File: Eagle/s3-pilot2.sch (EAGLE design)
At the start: 17 parts, among them J1 ARDUINO_R3_SHIELD, M2_1 ENA_JMP

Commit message: chkpt before changing ISR around - it is not working well - too fast?
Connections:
- new net 3.3: J1.3.3V, MPU6050.VCC
- net GND: now also J1.GND@0, J1.GND@1
- net VDD: no longer MPU6050.VCC
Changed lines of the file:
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@@
 <wire x1="241.3" y1="38.1" x2="241.3" y2="81.28" width="0.1524" layer="91"/>
 <pinref part="J1" gate="G$1" pin="GND@2"/>
-<wire x1="241.3" y1="81.28" x2="223.52" y2="81.28" width="0.1524" layer="91"/>
+<wire x1="241.3" y1="81.28" x2="228.6" y2="81.28" width="0.1524" layer="91"/>
+<wire x1="228.6" y1="81.28" x2="223.52" y2="81.28" width="0.1524" layer="91"/>
 <wire x1="241.3" y1="81.28" x2="241.3" y2="86.36" width="0.1524" layer="91"/>
 <junction x="241.3" y="81.28"/>
 <pinref part="GND2" gate="1" pin="GND"/>
+<pinref part="J1" gate="G$1" pin="GND@0"/>
+<wire x1="223.52" y1="86.36" x2="228.6" y2="86.36" width="0.1524" layer="91"/>
+<wire x1="228.6" y1="86.36" x2="228.6" y2="83.82" width="0.1524" layer="91"/>
+<junction x="228.6" y="81.28"/>
+<pinref part="J1" gate="G$1" pin="GND@1"/>
+<wire x1="228.6" y1="83.82" x2="228.6" y2="81.28" width="0.1524" layer="91"/>
+<wire x1="223.52" y1="83.82" x2="228.6" y2="83.82" width="0.1524" layer="91"/>
+<junction x="228.6" y="83.82"/>
 </segment>
 <segment>
@@
 <net name="VDD" class="1">
 <segment>
-<pinref part="MPU6050" gate="G$1" pin="VCC"/>
-<wire x1="160.02" y1="35.56" x2="243.84" y2="35.56" width="0.1524" layer="91"/>
-<wire x1="243.84" y1="35.56" x2="243.84" y2="73.66" width="0.1524" layer="91"/>
+<wire x1="243.84" y1="30.48" x2="243.84" y2="73.66" width="0.1524" layer="91"/>
 <pinref part="J1" gate="G$1" pin="5V"/>
 <wire x1="243.84" y1="73.66" x2="223.52" y2="73.66" width="0.1524" layer="91"/>
-<wire x1="243.84" y1="35.56" x2="243.84" y2="30.48" width="0.1524" layer="91"/>
-<junction x="243.84" y="35.56"/>
 <pinref part="SUPPLY1" gate="VDD" pin="VDD"/>
 </segment>
@@
 </segment>
 </net>
+<net name="3.3" class="0">
+<segment>
+<pinref part="J1" gate="G$1" pin="3.3V"/>
+<wire x1="223.52" y1="76.2" x2="228.6" y2="76.2" width="0.1524" layer="91"/>
+<label x="228.6" y="76.2" size="1.778" layer="95"/>
+</segment>
+<segment>
+<pinref part="MPU6050" gate="G$1" pin="VCC"/>
+<wire x1="160.02" y1="35.56" x2="170.18" y2="35.56" width="0.1524" layer="91"/>
+<label x="165.1" y="35.56" size="1.778" layer="95"/>
+</segment>
+</net>

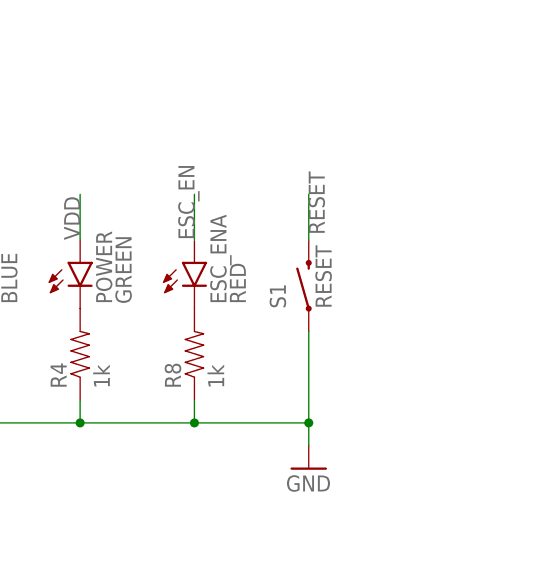
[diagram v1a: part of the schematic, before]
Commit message: working basically, still need to correct x/y/h stuff (as usual) added remote reset jumper for arduino to sch
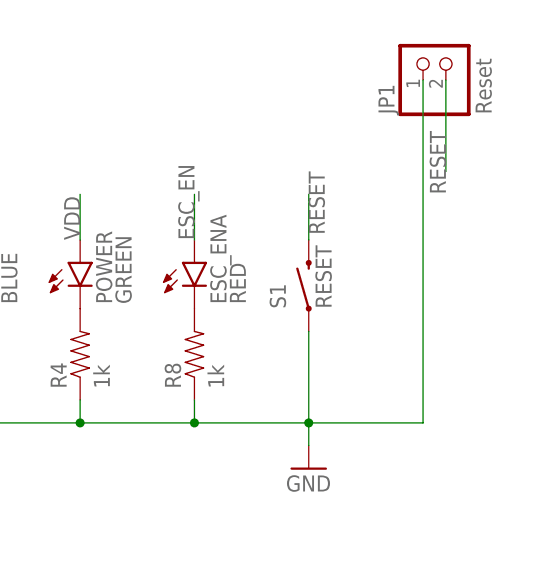
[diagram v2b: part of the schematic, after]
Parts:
- added JP1: Reset, pinhead:PINHD-1X2/90
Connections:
- net GND: now also JP1.1
- net RESET: now also JP1.2
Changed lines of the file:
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@@
 <part name="GND3" library="SparkFun-Aesthetics" deviceset="GND" device=""/>
 <part name="GND4" library="SparkFun-Aesthetics" deviceset="GND" device=""/>
+<part name="JP1" library="pinhead" deviceset="PINHD-1X2" device="/90" value="Reset"/>
 </parts>
 <sheets>
@@
 <instance part="GND3" gate="1" x="50.8" y="109.22" rot="R270"/>
 <instance part="GND4" gate="1" x="50.8" y="60.96" rot="R270"/>
+<instance part="JP1" gate="G$1" x="236.22" y="157.48" rot="R90"/>
 </instances>
 <busses>
@@
 <pinref part="GND1" gate="1" pin="GND"/>
 <pinref part="S1" gate="G$1" pin="1"/>
+<pinref part="JP1" gate="G$1" pin="1"/>
+<wire x1="220.98" y1="116.84" x2="233.68" y2="116.84" width="0.1524" layer="91"/>
+<wire x1="233.68" y1="116.84" x2="233.68" y2="154.94" width="0.1524" layer="91"/>
 </segment>
 <segment>
@@
 <label x="228.6" y="68.58" size="1.778" layer="95"/>
 </segment>
-</net>
+<segment>
+<pinref part="JP1" gate="G$1" pin="2"/>
+<wire x1="236.22" y1="154.94" x2="236.22" y2="144.78" width="0.1524" layer="91"/>
+<label x="236.22" y="142.24" size="1.778" layer="95" rot="R90"/>
+</segment>
+</net>

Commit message: eagle updates - brd not complete
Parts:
- removed S1: RESET, SparkFun-Electromechanical:SWITCH-MOMENTARY-2SMD-REDUNDANT
- added RESET: RESET, SparkFun-Electromechanical:SWITCH-MOMENTARY-2SMD-4
- JP1: device pinhead:PINHD-1X2/90 -> pinhead:PINHD-1X2
- M2_1: value ENA_JMP -> ENA
- U$1: value MC33926-SINGLE-BO -> M1
- renumbered ESC_ENA to ENABLE, J1 to GND
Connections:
- removed net N$1: GND.SCL, MPU6050.SCL
- removed net N$2: GND.SDA, MPU6050.SDA
- new net SCL: GND.A5, GND.SCL, MPU6050.SCL
- new net SDA: GND.A4, GND.SDA, MPU6050.SDA
- net GND: now also RESET.1; no longer S1.1
- net M1_FB: now also GND.A2; no longer GND.A0
- net RESET: now also RESET.2; no longer S1.2
